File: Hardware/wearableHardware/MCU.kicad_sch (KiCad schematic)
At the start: 26 parts, among them Q1 BSS138, Q2 MMBT2222A, SW1 SW_Push, SW2 SW_Push, SW3 SW_Push, U1 ESP32-S3-MINI-1

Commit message: feat: initialize KiCad hardware project with MCU schematic and pinmap configuration
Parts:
- removed D1: 1N4148W, Diode_SMD:D_SOD-123, symbol Diode:1N4148W
- removed Q1: BSS138, Package_TO_SOT_SMD:SOT-23, symbol Transistor_FET:BSS138
- removed Q2: MMBT2222A, Package_TO_SOT_SMD:SOT-23, symbol Transistor_BJT:MMBT2222A
- removed R10, R11: 22, Resistor_SMD:R_0402_1005Metric, symbol Device:R
- removed R7, R8: 100k, Resistor_SMD:R_0402_1005Metric, symbol Device:R
- removed R9: 1k, Resistor_SMD:R_0402_1005Metric, symbol Device:R
- removed SW3: SW_Push, Button_Switch_SMD:SW_SPST_SKQG_WithStem, symbol Switch:SW_Push
- removed TP1, TP2, TP3, TP4: TestPoint, TestPoint:TestPoint_Pad_D1.0mm, symbol Connector_Generic:Conn_01x01
- added J1: USB_C_Receptacle_USB2.0_16P, Connector_USB:USB_C_Receptacle_GCT_USB4110, symbol Connector:USB_C_Receptacle_USB2.0_16P
- added R? (x2): 10k, Resistor_SMD:R_0402_1005Metric, symbol Device:R
- added U2: USBLC6-2SC6, Package_TO_SOT_SMD:SOT-23-6, symbol Power_Protection:USBLC6-2SC6
- C2: footprint Capacitor_SMD:C_0603_1608Metric -> Capacitor_SMD:C_0603_1608Metric_Pad1.08x0.95mm_HandSolder
- C3: value 1uF -> 100nF
- R1, R2: value 10k -> 4.7k
- R3, R4: value 4.7k -> 5.1k; footprint Resistor_SMD:R_0402_1005Metric -> (none)
- R5: value 1k -> 22
- R6: value 15 -> 22
- SW1, SW2: footprint Button_Switch_SMD:SW_SPST_SKQG_WithStem -> (none)
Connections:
- net BTN_EVENT: now also U1.13 (IO9)
- net DRDY: now also U1.20 (IO16)
- net HAPTIC_PWM: now also U1.14 (IO10)
- net I2C_SCL: now also R2.2, U1.6 (IO2)
- net I2C_SDA: now also R1.2, U1.5 (IO1)
- net SPI1_CLK: now also U1.17 (IO13)
- net SPI1_CS: now also U1.19 (IO15)
- net SPI1_MISO: now also U1.18 (IO14)
- net SPI1_MOSI: now also U1.16 (IO12)
- net SPI2_BLK: now also U1.30 (IO48)
- net SPI2_CS: now also U1.31 (IO35)
- net SPI2_DC: now also U1.32 (IO36)
- net SPI2_MOSI: now also U1.35 (IO39)
- net SPI2_RST: now also U1.33 (IO37)
- net SPI2_SCLK: now also U1.34 (IO38)
- net GND: now reaches U1.1 (GND), U1.2 (GND), U1.42 (GND), U1.43 (GND), U1.46 (GND), U1.47 (GND), U1.48 (GND), U1.49 (GND), U1.50 (GND), U1.51 (GND), U1.52 (GND), U1.53 (GND), U1.54 (GND), U1.55 (GND), U1.56 (GND), U1.57 (GND), U1.58 (GND), U1.59 (GND), U1.60 (GND), U1.61 (GND), U1.62 (GND), U1.63 (GND), U1.64 (GND), U1.65 (GND)
- net GND: now also C1.2, C2.2, C3.2, C4.2, R3.2, R4.2, SW1.2, SW2.1, J1.A1 (GND), J1.A12 (GND), J1.B1 (GND), J1.B12 (GND), U2.2 (GND)
- net VBAT_FB: now reaches U1.12 (IO8)
- net at U1.23 (USB_D-): now also U2.3 (I/O2)
- net at U1.24 (USB_D+): now also U2.1 (I/O1)
- net +3.3V: now reaches U1.3 (3V3)
- net +3.3V: now also C1.1, C2.1, R1.1, R2.1, R?.1, R?.1
- net TOUCH_SDA: now reaches U1.36 (IO40)
- net TOUCH_SCL: now reaches U1.37 (IO41)
- net at U1.4 (IO0): now also SW2.2, R?.2
- net at U1.45 (EN): now also C3.1, SW1.1, R?.2
- new net: R5.1, R6.1, U2.4 (I/O2), U2.6 (I/O1)
- new net: J1.A6 (D+), J1.B6 (D+), R5.2
- new net: C4.1, J1.A4 (VBUS), J1.A9 (VBUS), J1.B4 (VBUS), J1.B9 (VBUS), U2.5 (VBUS)
- new net: J1.A5 (CC1), R3.1
- new net: J1.A7 (D-), J1.B7 (D-), R6.2
- new net: J1.B5 (CC2), R4.1

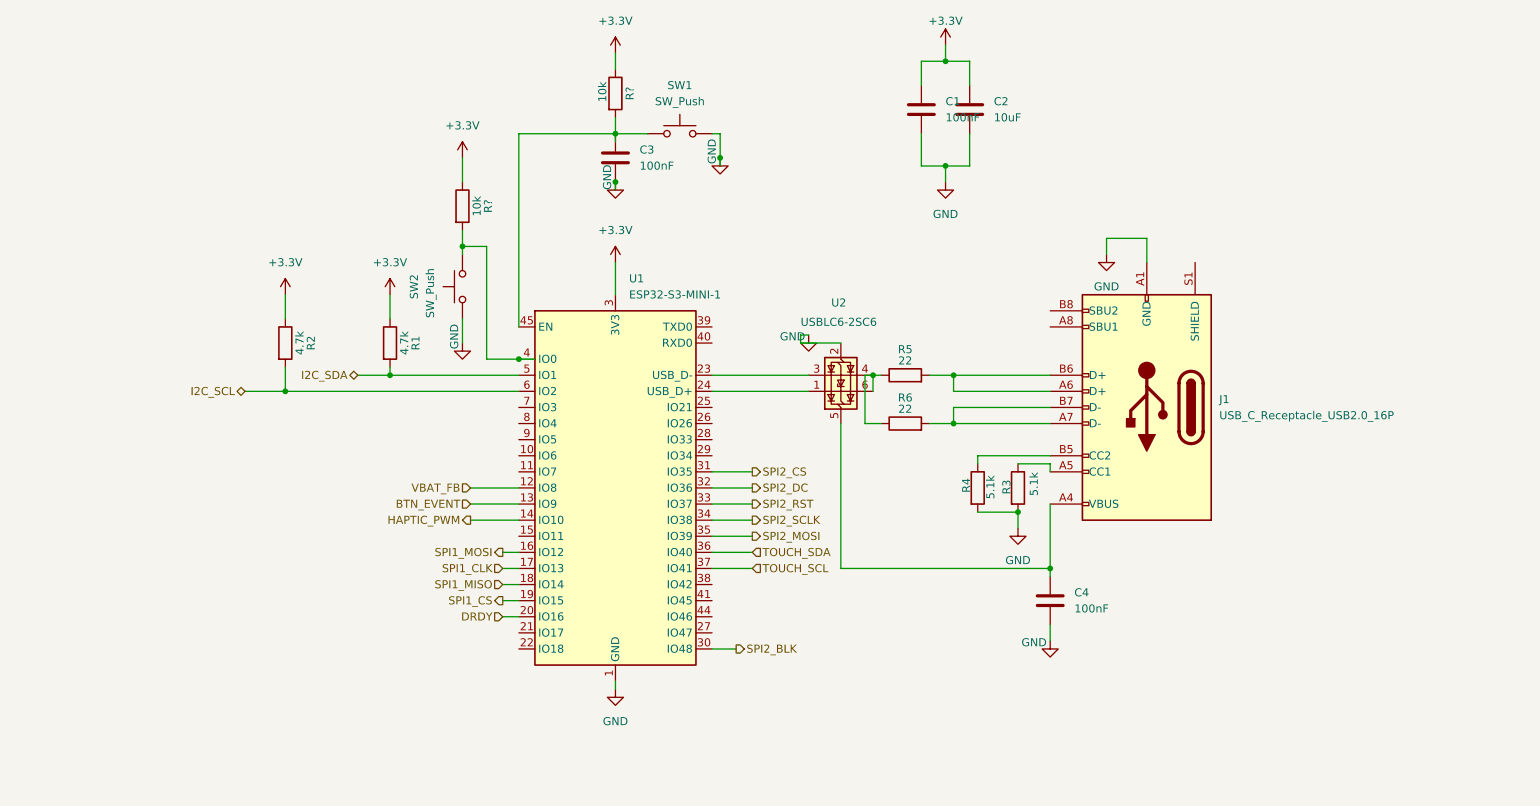
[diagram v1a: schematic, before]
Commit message: feat: add hardware schematics, documentation images, and external component libraries for wearable device development
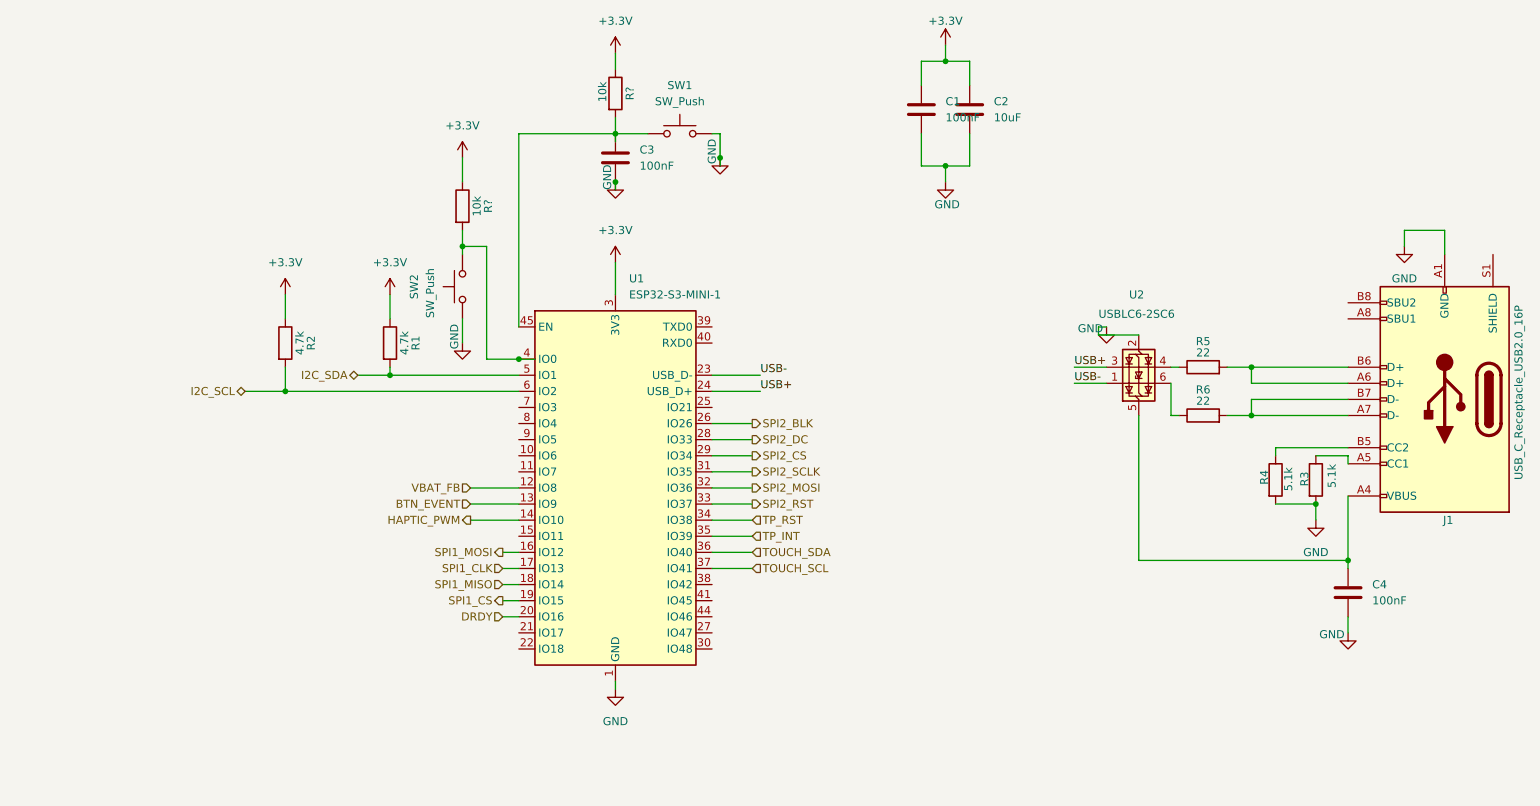
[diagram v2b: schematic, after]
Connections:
- net SPI2_BLK: now also U1.26 (IO26); no longer U1.30 (IO48)
- net SPI2_CS: now also U1.29 (IO34); no longer U1.31 (IO35)
- net SPI2_DC: now also U1.28 (IO33); no longer U1.32 (IO36)
- net SPI2_MOSI: now also U1.32 (IO36); no longer U1.35 (IO39)
- net SPI2_SCLK: now also U1.31 (IO35); no longer U1.34 (IO38)
- net at R5.1, U2.4 (I/O2): no longer R6.1, U2.6 (I/O1)
- net USB+: now reaches U2.3 (I/O2)
- net USB+: now also U1.24 (USB_D+); no longer U1.23 (USB_D-)
- net USB-: now reaches U2.1 (I/O1)
- net USB-: now also U1.23 (USB_D-); no longer U1.24 (USB_D+)
- new net: R6.1, U2.6 (I/O1)
- new net TP_INT: U1.35 (IO39)
- new net TP_RST: U1.34 (IO38)
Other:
- moved on the sheet: C4, J1, R3, R4, R5, R6, U2
